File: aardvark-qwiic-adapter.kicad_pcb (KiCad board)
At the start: 2 copper layers, 22.9 x 20.3 mm, 7 parts, among them J1 Conn_02x05_Odd_Even, J2 Conn_01x04, J3 Conn_01x04, J4 Conn_01x02, U1 AP7361C-33E

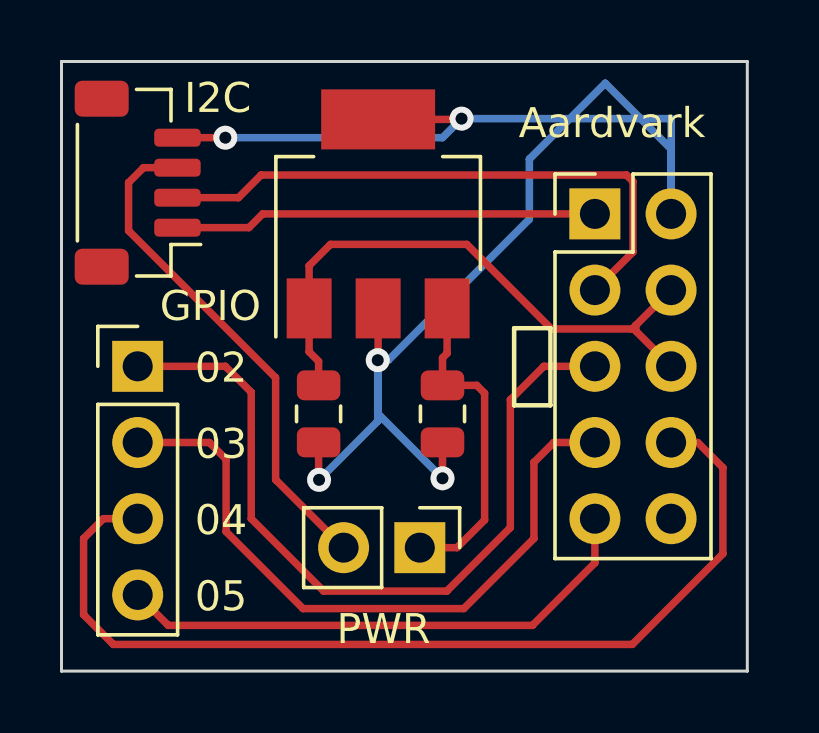
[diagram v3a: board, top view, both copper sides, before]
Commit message: Fix backwards QWIIC
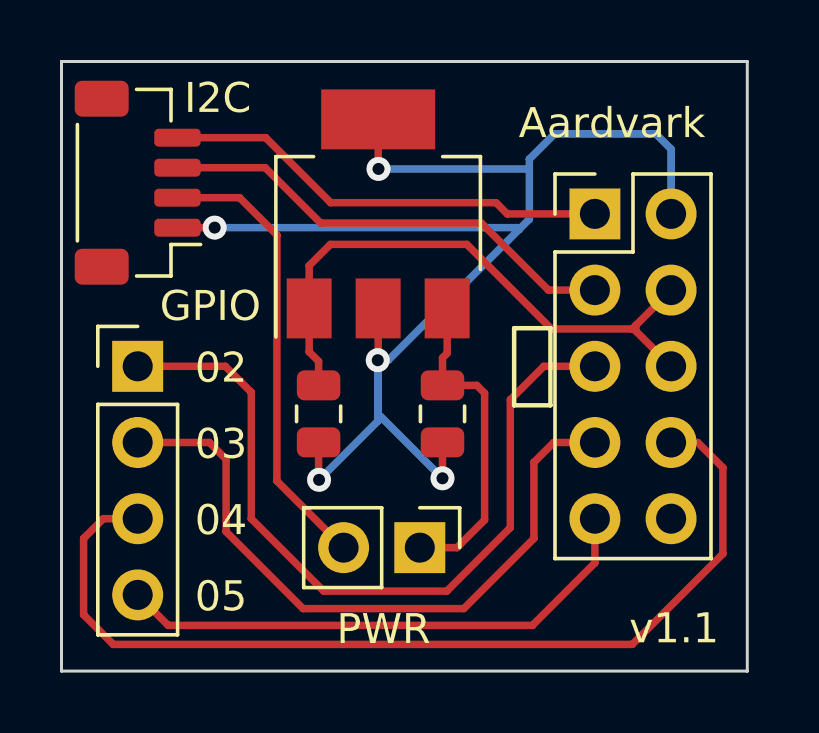
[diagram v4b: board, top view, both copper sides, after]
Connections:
- J2 pad 1: /SCL -> GND
- J2 pad 2: /SDA -> /PWR
- J2 pad 3: /PWR -> /SDA
- J2 pad 4: GND -> /SCL
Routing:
- net GND: track 54.3 -> 48.4 mm
- net /SDA: track 19.7 -> 15.6 mm
- net /PWR: track 17.0 -> 15.2 mm
- net /SCL: track 14.1 -> 15.0 mm
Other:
- board text added: "v1.1"
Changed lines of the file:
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@@
   (title_block
     (title "Aardvark QUIIC Adapter")
-    (date "2023-02-19")
-    (rev "1.0")
+    (date "2023-02-22")
+    (rev "1.1")
   )
   (layers
@@
       (stroke (width 0.1) (type solid)) (layer "F.Fab"))
     (pad "1" smd roundrect (at -1.5 1.325 90) (size 0.6 1.55) (layers "F.Cu" "F.Paste" "F.Mask") (roundrect_rratio 0.25)
-      (net 1 "/SCL") (pinfunction "Pin_1") (pintype "passive"))
+      (net 3 "GND") (pinfunction "Pin_1") (pintype "passive"))
     (pad "2" smd roundrect (at -0.5 1.325 90) (size 0.6 1.55) (layers "F.Cu" "F.Paste" "F.Mask") (roundrect_rratio 0.25)
-      (net 2 "/SDA") (pinfunction "Pin_2") (pintype "passive"))
+      (net 9 "/PWR") (pinfunction "Pin_2") (pintype "passive"))
     (pad "3" smd roundrect (at 0.5 1.325 90) (size 0.6 1.55) (layers "F.Cu" "F.Paste" "F.Mask") (roundrect_rratio 0.25)
-      (net 9 "/PWR") (pinfunction "Pin_3") (pintype "passive"))
+      (net 2 "/SDA") (pinfunction "Pin_3") (pintype "passive"))
     (pad "4" smd roundrect (at 1.5 1.325 90) (size 0.6 1.55) (layers "F.Cu" "F.Paste" "F.Mask") (roundrect_rratio 0.25)
-      (net 3 "GND") (pinfunction "Pin_4") (pintype "passive"))
+      (net 1 "/SCL") (pinfunction "Pin_4") (pintype "passive"))
     (pad "MP" smd roundrect (at -2.8 -1.2 90) (size 1.2 1.8) (layers "F.Cu" "F.Paste" "F.Mask") (roundrect_rratio 0.208333))
     (pad "MP" smd roundrect (at 2.8 -1.2 90) (size 1.2 1.8) (layers "F.Cu" "F.Paste" "F.Mask") (roundrect_rratio 0.208333))
@@
     (effects (font (size 1 1) (thickness 0.15)) (justify left bottom))
   )
-  (segment (start 132.08 81.28) (end 121.0056 81.28) (width 0.25) (layer "F.Cu") (net 1))
-  (segment (start 118.1678 81.7372) (end 118.165 81.74) (width 0.25) (layer "F.Cu") (net 1))
-  (segment (start 121.0056 81.28) (end 120.5484 81.7372) (width 0.25) (layer "F.Cu") (net 1))
-  (segment (start 120.5484 81.7372) (end 118.1678 81.7372) (width 0.25) (layer "F.Cu") (net 1))
-  (segment (start 133.1346 79.9846) (end 120.9548 79.9846) (width 0.25) (layer "F.Cu") (net 2))
-  (segment (start 132.08 83.82) (end 133.35 82.55) (width 0.25) (layer "F.Cu") (net 2))
-  (segment (start 133.35 80.2) (end 133.1346 79.9846) (width 0.25) (layer "F.Cu") (net 2))
-  (segment (start 133.35 82.55) (end 133.35 80.2) (width 0.25) (layer "F.Cu") (net 2))
-  (segment (start 120.9548 79.9846) (end 120.1994 80.74) (width 0.25) (layer "F.Cu") (net 2))
-  (segment (start 120.1994 80.74) (end 118.165 80.74) (width 0.25) (layer "F.Cu") (net 2))
-  (segment (start 118.165 78.74) (end 119.761 78.74) (width 0.25) (layer "F.Cu") (net 3))
+  (gr_text "v1.1" (at 133.223 95.6818) (layer "F.SilkS")
+    (effects (font (size 1 1) (thickness 0.15)) (justify left bottom))
+  )
+  (segment (start 129.159 81.28) (end 132.08 81.28) (width 0.25) (layer "F.Cu") (net 1))
+  (segment (start 128.7852 80.9062) (end 129.159 81.28) (width 0.25) (layer "F.Cu") (net 1))
+  (segment (start 121.1072 78.74) (end 123.2734 80.9062) (width 0.25) (layer "F.Cu") (net 1))
+  (segment (start 118.165 78.74) (end 121.1072 78.74) (width 0.25) (layer "F.Cu") (net 1))
+  (segment (start 123.2734 80.9062) (end 128.7852 80.9062) (width 0.25) (layer "F.Cu") (net 1))
+  (segment (start 118.165 79.74) (end 121.0912 79.74) (width 0.25) (layer "F.Cu") (net 2))
+  (segment (start 128.2954 81.5848) (end 130.5306 83.82) (width 0.25) (layer "F.Cu") (net 2))
+  (segment (start 121.0912 79.74) (end 122.936 81.5848) (width 0.25) (layer "F.Cu") (net 2))
+  (segment (start 122.936 81.5848) (end 128.2954 81.5848) (width 0.25) (layer "F.Cu") (net 2))
+  (segment (start 130.5306 83.82) (end 132.08 83.82) (width 0.25) (layer "F.Cu") (net 2))
+  (segment (start 124.855 79.77) (end 124.8664 79.7814) (width 0.25) (layer "F.Cu") (net 3))
+  (segment (start 119.4026 81.74) (end 119.4054 81.7372) (width 0.25) (layer "F.Cu") (net 3))
   (segment (start 122.87 88.895) (end 122.87 90.1294) (width 0.25) (layer "F.Cu") (net 3))
+  (segment (start 118.165 81.74) (end 119.4026 81.74) (width 0.25) (layer "F.Cu") (net 3))
   (segment (start 122.87 90.1294) (end 122.8852 90.1446) (width 0.25) (layer "F.Cu") (net 3))
-  (segment (start 124.855 78.13) (end 127.61 78.13) (width 0.25) (layer "F.Cu") (net 3))
-  (segment (start 127.61 78.13) (end 127.635 78.105) (width 0.25) (layer "F.Cu") (net 3))
+  (segment (start 124.855 78.13) (end 124.855 79.77) (width 0.25) (layer "F.Cu") (net 3))
   (segment (start 124.855 86.1428) (end 124.841 86.1568) (width 0.25) (layer "F.Cu") (net 3))
   (segment (start 124.855 84.43) (end 124.855 86.1428) (width 0.25) (layer "F.Cu") (net 3))
   (segment (start 127 88.895) (end 127 90.0938) (width 0.25) (layer "F.Cu") (net 3))
-  (via (at 127.635 78.105) (size 0.8) (drill 0.4) (layers "F.Cu" "B.Cu") (net 3))
   (via (at 122.8852 90.1446) (size 0.8) (drill 0.4) (layers "F.Cu" "B.Cu") (net 3))
+  (via (at 124.8664 79.7814) (size 0.8) (drill 0.4) (layers "F.Cu" "B.Cu") (net 3))
   (via (at 127 90.0938) (size 0.8) (drill 0.4) (layers "F.Cu" "B.Cu") (net 3))
-  (via (at 119.761 78.74) (size 0.8) (drill 0.4) (layers "F.Cu" "B.Cu") (net 3))
+  (via (at 119.4054 81.7372) (size 0.8) (drill 0.4) (layers "F.Cu" "B.Cu") (net 3))
   (via (at 124.841 86.1568) (size 0.8) (drill 0.4) (layers "F.Cu" "B.Cu") (net 3))
-  (segment (start 129.8956 81.4578) (end 129.8956 79.4512) (width 0.25) (layer "B.Cu") (net 3))
+  (segment (start 125.1966 86.1568) (end 129.5527 81.8007) (width 0.25) (layer "B.Cu") (net 3))
   (segment (start 122.8852 90.1446) (end 124.841 88.1888) (width 0.25) (layer "B.Cu") (net 3))
-  (segment (start 134.62 78.105) (end 134.62 81.28) (width 0.25) (layer "B.Cu") (net 3))
-  (segment (start 129.8956 79.4512) (end 132.4229 76.9239) (width 0.25) (layer "B.Cu") (net 3))
+  (segment (start 134.112 78.613) (end 134.62 79.121) (width 0.25) (layer "B.Cu") (net 3))
+  (segment (start 119.4054 81.7372) (end 129.4892 81.7372) (width 0.25) (layer "B.Cu") (net 3))
+  (segment (start 129.8956 81.4578) (end 129.8956 79.7814) (width 0.25) (layer "B.Cu") (net 3))
+  (segment (start 130.7338 78.613) (end 134.112 78.613) (width 0.25) (layer "B.Cu") (net 3))
+  (segment (start 124.841 88.1888) (end 124.841 86.1568) (width 0.25) (layer "B.Cu") (net 3))
+  (segment (start 129.8956 79.4512) (end 130.7338 78.613) (width 0.25) (layer "B.Cu") (net 3))
   (segment (start 134.62 79.121) (end 134.62 81.28) (width 0.25) (layer "B.Cu") (net 3))
-  (segment (start 124.841 88.1888) (end 124.841 86.1568) (width 0.25) (layer "B.Cu") (net 3))
-  (segment (start 125.1966 86.1568) (end 129.8956 81.4578) (width 0.25) (layer "B.Cu") (net 3))
+  (segment (start 124.8664 79.7814) (end 129.8956 79.7814) (width 0.25) (layer "B.Cu") (net 3))
   (segment (start 124.841 86.1568) (end 125.1966 86.1568) (width 0.25) (layer "B.Cu") (net 3))
-  (segment (start 127 78.74) (end 127.635 78.105) (width 0.25) (layer "B.Cu") (net 3))
   (segment (start 124.841 87.9348) (end 124.841 86.1568) (width 0.25) (layer "B.Cu") (net 3))
-  (segment (start 119.761 78.74) (end 127 78.74) (width 0.25) (layer "B.Cu") (net 3))
-  (segment (start 132.4229 76.9239) (end 134.62 79.121) (width 0.25) (layer "B.Cu") (net 3))
-  (segment (start 127.635 78.105) (end 134.62 78.105) (width 0.25) (layer "B.Cu") (net 3))
+  (segment (start 129.5527 81.8007) (end 129.8956 81.4578) (width 0.25) (layer "B.Cu") (net 3))
+  (segment (start 129.4892 81.7372) (end 129.5527 81.8007) (width 0.25) (layer "B.Cu") (net 3))
+  (segment (start 129.8956 79.7814) (end 129.8956 79.4512) (width 0.25) (layer "B.Cu") (net 3))
   (segment (start 127 90.0938) (end 124.841 87.9348) (width 0.25) (layer "B.Cu") (net 3))
   (segment (start 127.155 85.9256) (end 127.155 84.43) (width 0.25) (layer "F.Cu") (net 4))
@@
   (segment (start 129.9972 94.996) (end 117.856 94.996) (width 0.25) (layer "F.Cu") (net 8))
   (segment (start 132.08 92.9132) (end 129.9972 94.996) (width 0.25) (layer "F.Cu") (net 8))
-  (segment (start 118.165 79.74) (end 117.0338 79.74) (width 0.25) (layer "F.Cu") (net 9))
-  (segment (start 116.5352 81.8388) (end 121.4374 86.741) (width 0.25) (layer "F.Cu") (net 9))
-  (segment (start 117.0338 79.74) (end 116.5352 80.2386) (width 0.25) (layer "F.Cu") (net 9))
-  (segment (start 121.4374 86.741) (end 121.4374 90.1396) (width 0.25) (layer "F.Cu") (net 9))
-  (segment (start 116.5352 80.2386) (end 116.5352 81.8388) (width 0.25) (layer "F.Cu") (net 9))
-  (segment (start 121.4374 90.1396) (end 123.703 92.4052) (width 0.25) (layer "F.Cu") (net 9))
+  (segment (start 121.48 90.1822) (end 121.48 81.983) (width 0.25) (layer "F.Cu") (net 9))
+  (segment (start 120.237 80.74) (end 118.165 80.74) (width 0.25) (layer "F.Cu") (net 9))
+  (segment (start 123.703 92.4052) (end 121.48 90.1822) (width 0.25) (layer "F.Cu") (net 9))
+  (segment (start 121.48 81.983) (end 120.237 80.74) (width 0.25) (layer "F.Cu") (net 9))
   (segment (start 134.62 83.82) (end 133.445 84.995) (width 0.25) (layer "F.Cu") (net 10))
   (segment (start 133.445 84.995) (end 133.3246 85.1154) (width 0.25) (layer "F.Cu") (net 10))
